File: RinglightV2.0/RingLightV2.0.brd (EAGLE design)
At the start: 47 x 47 mm, 17 parts, among them P1 M-1X02-SIP-100-32Y

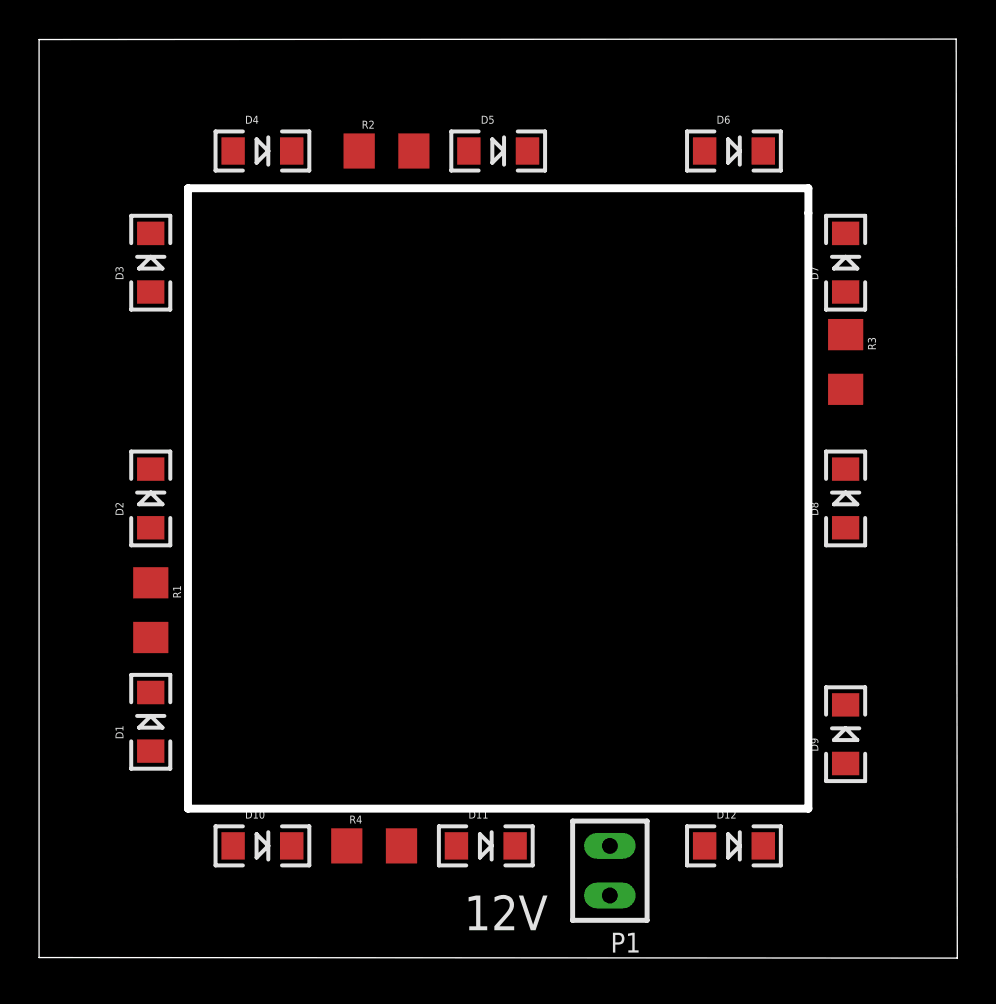
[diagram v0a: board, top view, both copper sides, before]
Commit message: Pushed routed board, realized version from yesterday hadn't been routed
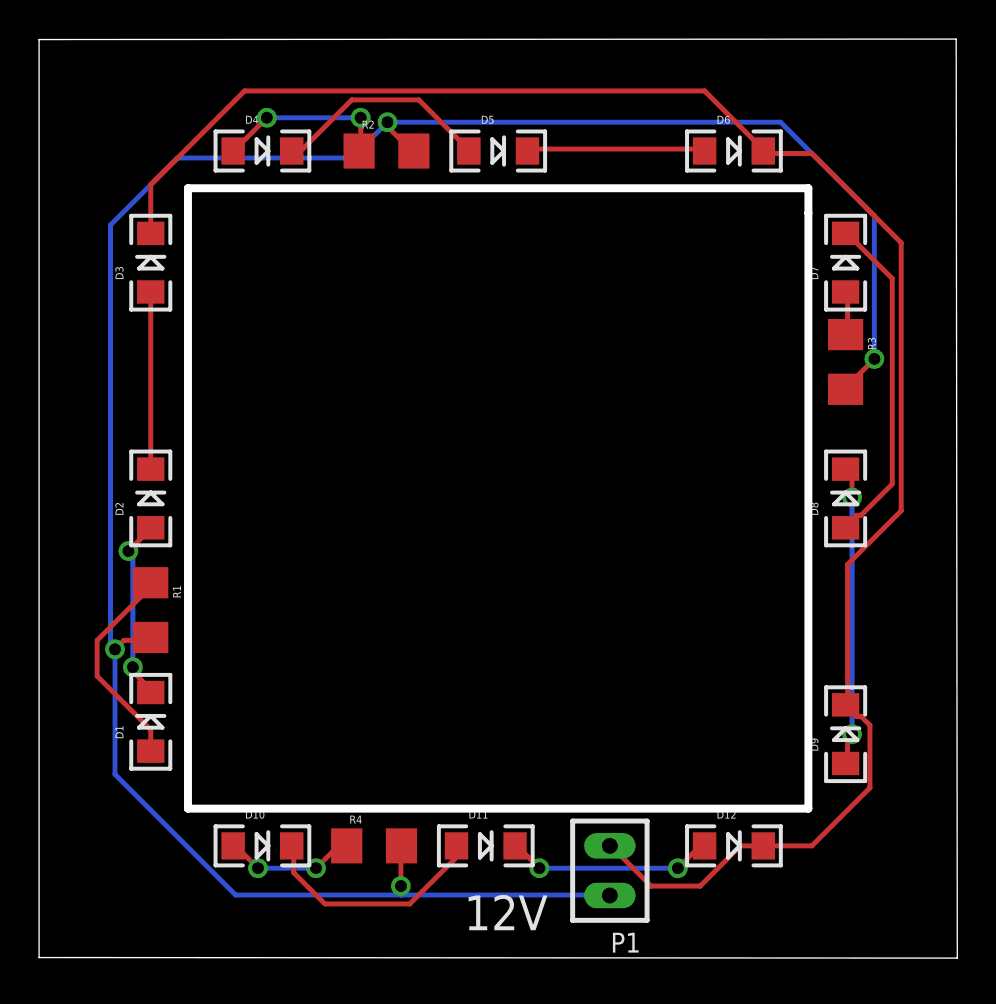
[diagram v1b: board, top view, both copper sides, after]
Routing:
- net VCC: track 0.00 -> 115.6 mm, vias 0 -> 4
- net GND: track 0.00 -> 92.1 mm
- net N$7: track 0.00 -> 17.2 mm
- net N$10: track 0.00 -> 15.3 mm, vias 0 -> 2
- net N$8: track 0.00 -> 12.1 mm
- net N$6: track 0.00 -> 11.3 mm
- net N$1: track 0.00 -> 10.9 mm
- net N$9: track 0.00 -> 10.6 mm, vias 0 -> 2
- net N$5: track 0.00 -> 9.38 mm, vias 0 -> 2
- net N$11: track 0.00 -> 9.12 mm
- net N$12: track 0.00 -> 9.07 mm
- net N$2: track 0.00 -> 8.96 mm, vias 0 -> 2
- net N$4: track 0.00 -> 6.76 mm, vias 0 -> 2
- net N$3: track 0.00 -> 2.24 mm
